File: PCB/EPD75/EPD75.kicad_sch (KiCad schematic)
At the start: 122 parts, among them J1 Conn_01x26, J10 TF_PUSH, J11 Reset, J12 TC2030-USB-NL-DS, J4 BTN1, J5 USB-C-Socket-V, J7 USB-C-Socket-V, J8 PWR, Q1 BSS138, U3 MD8942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

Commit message: PCB updatep
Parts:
- removed C21: 10uF 35V, RevK:C_0603_, symbol RevK:Hidden
- removed C49: 10uF 6.3V, RevK:C_0603_, symbol RevK:Hidden
- removed C50: 100nF, RevK:C_0603_, symbol RevK:Hidden
- removed JP2: SolderJumper_3_Bridged12, RevK:SolderJumper3, symbol Jumper:SolderJumper_3_Bridged12
- removed L3: 10uH, RevK:L_4x4_, symbol RevK:Hidden
- removed R15: 124k, RevK:R_0402_, symbol RevK:Hidden
- removed R16: 39k2, RevK:R_0402_, symbol RevK:Hidden
- removed R17: 1M, RevK:R_0402_, symbol RevK:Hidden
- removed R2: 3R, RevK:R_0402, symbol Device:R
- removed U5: MD8942, RevK:SOT-23-6-MD8942, symbol RevK:MD89420-RegBlock
- C17, C18: value 4.7uF -> 4.7uF 50V; footprint RevK:C_0402 -> RevK:C_0805
- L1: value 10uH -> 470uH; footprint RevK:L_4x4 -> Inductor_SMD:L_Ferrocore_DLG-0705
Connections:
- net EPOWER is gone; now on net +3.3V: C11.1, C18.2, C42.1, C51.2, C52.2, C53.2, J1.15 (Pin_15), J1.16 (Pin_16), JP1.3 (B), L1.2
- net at R1.1: now also J1.3 (Pin_3), Q1.2 (S)
- net EPWR: no longer names the net of U4.29 (GPIO34)
- no-connect marks 24 -> 25
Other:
- moved on the sheet: R1

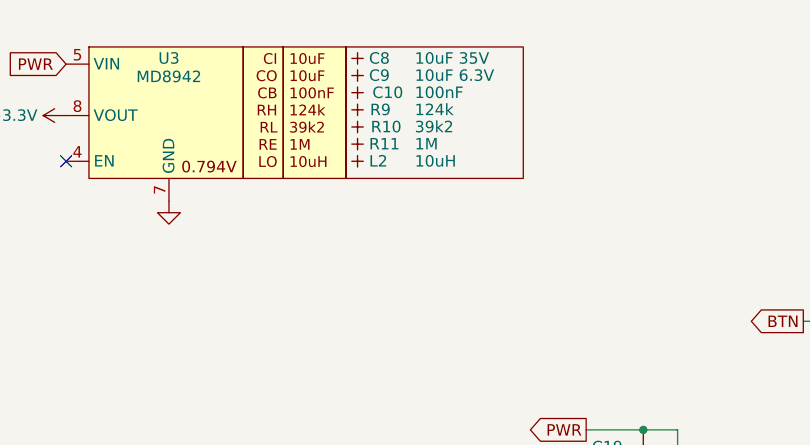
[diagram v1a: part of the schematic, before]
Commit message: Render and PCB tidy (inductors)
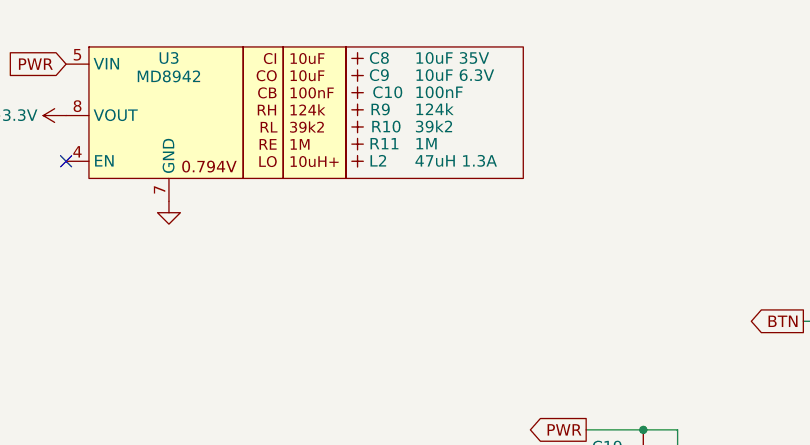
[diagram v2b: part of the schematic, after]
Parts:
- L1: footprint Inductor_SMD:L_Ferrocore_DLG-0705 -> RevK:L_4x4; MPN (none) -> C42429207
- L2: value 10uH -> 47uH 1.3A; MPN (none) -> C602032
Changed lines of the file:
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@@
 			)
 		)
-		(property "Description" ""
+		(property "Description" "Regulator and associated components."
 			(at 159.385 26.035 0)
 			(effects
@@
 			)
 		)
-		(property "Value" "10uH"
+		(property "Value" "47uH 1.3A"
 			(at 186.69 31.115 90)
 			(effects
@@
 			)
 		)
-		(property "Part No" ""
-			(at 180.34 31.115 0)
-			(effects
-				(font
-					(size 1.27 1.27)
-				)
-				(hide yes)
-			)
-		)
-		(property "Note" ""
-			(at 180.34 31.115 0)
+		(property "MPN" "C602032"
+			(at 180.34 31.115 90)
 			(effects
 				(font
@@
 			)
 		)
-		(property "Footprint" "Inductor_SMD:L_Ferrocore_DLG-0705"
+		(property "Footprint" "RevK:L_4x4"
 			(at 187.96 92.075 0)
 			(effects
@@
 			(at 187.96 92.075 0)
 			(effects
+				(font
+					(size 1.27 1.27)
+				)
+				(hide yes)
+			)
+		)
+		(property "MPN" "C42429207"
+			(at 187.96 92.075 0)
+			(effects

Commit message: Library update
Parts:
- L2: value 47uH 1.3A -> 10uH; MPN C602032 -> C42428017
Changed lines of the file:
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@@
 			)
 		)
-		(property "Value" "47uH 1.3A"
+		(property "Value" "10uH"
 			(at 186.69 31.115 90)
 			(effects
@@
 			)
 		)
-		(property "MPN" "C602032"
+		(property "MPN" "C42428017"
 			(at 180.34 31.115 90)
 			(effects

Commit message: Tidy
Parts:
- L2: MPN C42428017 -> C167879
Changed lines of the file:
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@@
 			)
 		)
-		(property "MPN" "C42428017"
+		(property "MPN" "C167879"
 			(at 180.34 31.115 90)
 			(effects
